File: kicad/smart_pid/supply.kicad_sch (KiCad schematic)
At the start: 67 parts, among them J5 Screw_Terminal_01x04, J6 Screw_Terminal_01x03, SW10 SW_DPDT_x2, U10 LM2940CS-5.0, U14 LM2940CS-12/NOPB, U15 LM2990SX-12, U16 LM317_TO-252, U18 LM2990SX-5.0, U27 MIC5205YM5, U30 MIC5271YM5

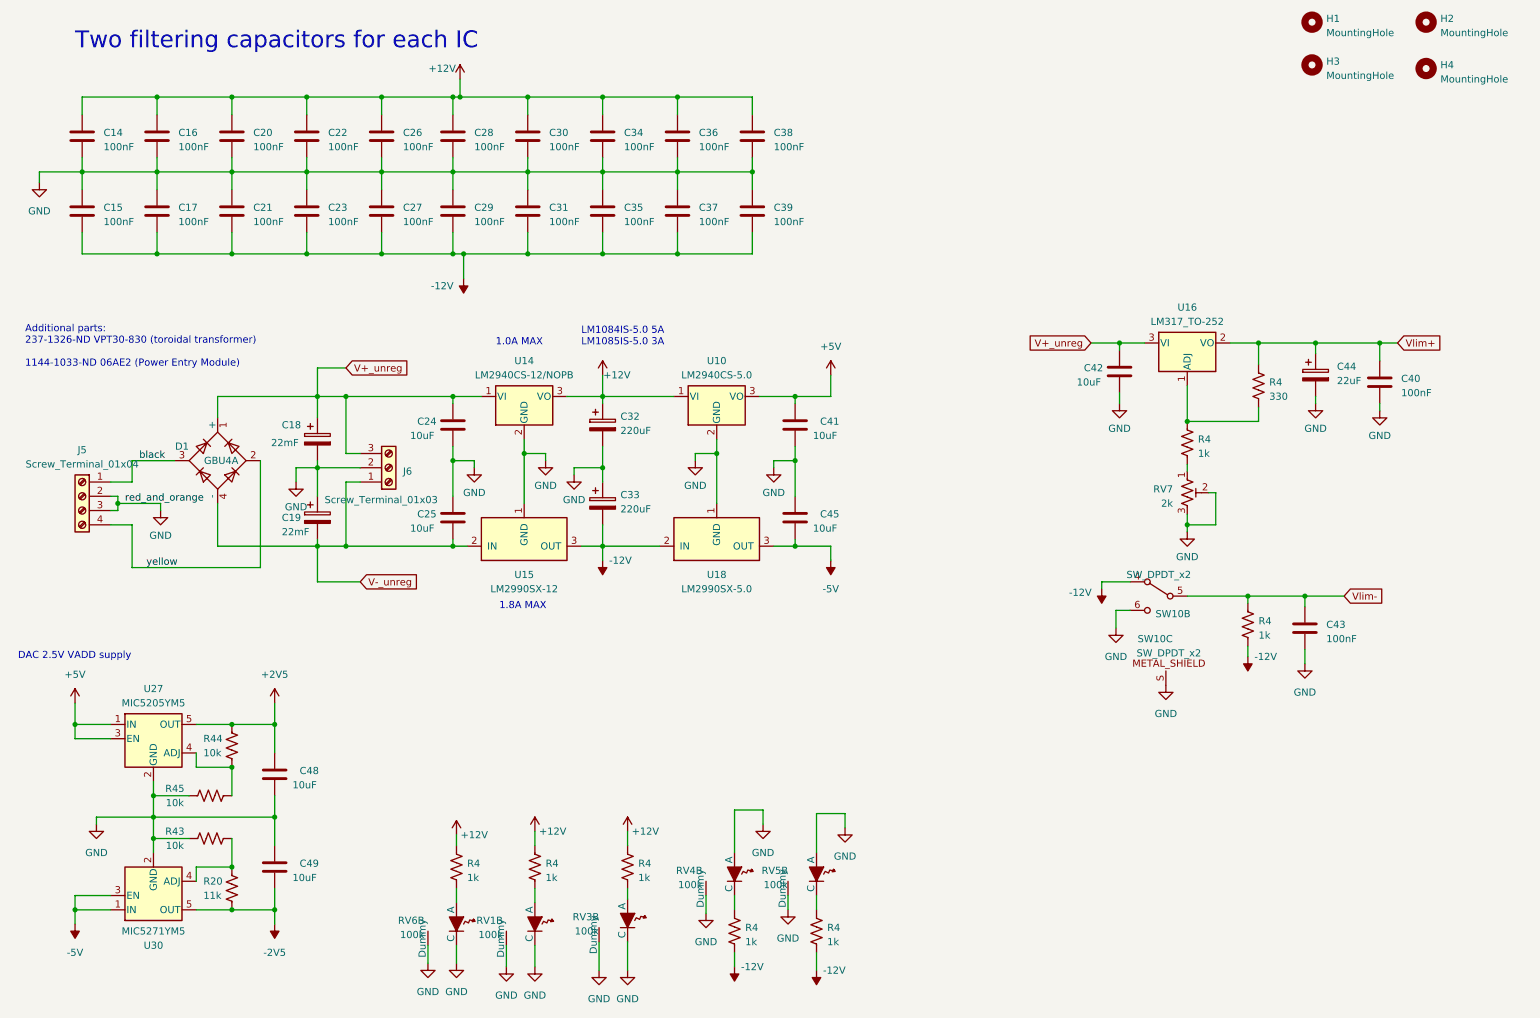
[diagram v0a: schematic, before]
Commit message: Added inverter and modified ext. setpoint disable
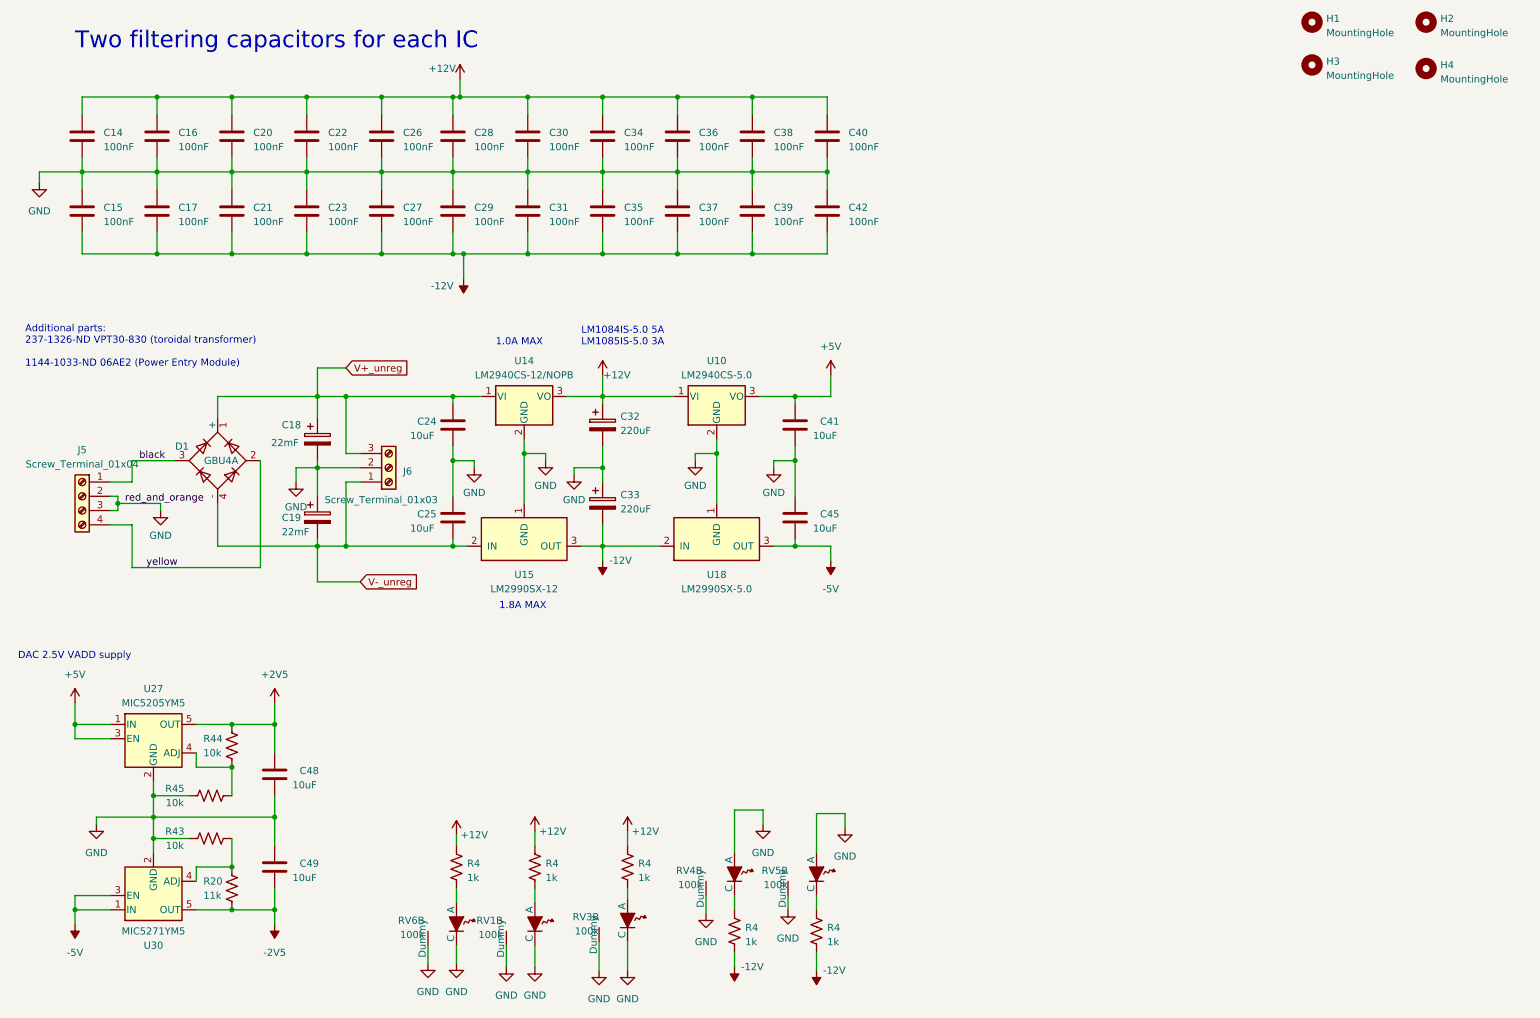
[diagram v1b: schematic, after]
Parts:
- removed C43: 100nF, Capacitor_SMD:C_0805_2012Metric, symbol Device:C
- removed C44: 22uF, Capacitor_SMD:CP_Elec_4x5.8, symbol Device:C_Polarized
- removed R4 (x2): 1k, Resistor_SMD:R_0805_2012Metric, symbol Device:R_US
- removed R4: 330, Resistor_SMD:R_0805_2012Metric, symbol Device:R_US
- removed RV7: 2k, Potentiometer_THT:Potentiometer_Bourns_3296W_Vertical, symbol Device:R_Potentiometer_Trim_US
- removed SW10: SW_DPDT_x2, lib:MHS222, symbol local_lib:SW_DPDT_x2
- removed U16: LM317_TO-252, Package_TO_SOT_SMD:TO-252-2, symbol Regulator_Linear:LM317_TO-252
- C42: value 10uF -> 100nF; footprint Capacitor_SMD:C_1210_3225Metric -> Capacitor_SMD:C_0805_2012Metric
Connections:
- net Vlim+ is gone; now on net +12V: C40.1
- net -12V: now also C42.2
- net GND: now also C42.1; no longer C42.2
- net V+_unreg: no longer C42.1
